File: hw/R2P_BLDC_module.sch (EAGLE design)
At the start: 59 parts, among them Q1 OPTIMOS, Q2 OPTIMOS, Q3 OPTIMOS, Q4 OPTIMOS, Q5 OPTIMOS, Q6 OPTIMOS, U1 STM32F103CX, U5 LD3985XX, X1 MICROMATCH-4

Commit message: H-bridge layout almost done
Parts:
- removed R3: 100k, rcl:R-EU_R0603
- removed U5: LD3985XX, st:LD3985XX
- added C14, C15, C16, C17: 100n, rcl:C-EUC0603
- added R11, R12: (no value), rcl:R-EU_R1206
- added R13, R14: 10, rcl:R-EU_R0603
- added U$10, U$12: INA193DBV, texas-instruments:INA193DBV
- added U$11: TPS73033, texas-instruments:TPS73033
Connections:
- net PWMAH renamed AH
- net PWMAL renamed AL
- removed net N$3: R3.2, U$1.TRI
- removed net PWMBH: U$8.PWMH
- removed net PWMBL: U$8.PWML
- removed net PWMCH: U$9.PWMH
- removed net PWMCL: U$9.PWML
- new net +A3V3: C14.1, C15.1, U$10SUPPLY.V+, U$12SUPPLY.V+, U1.VDD_A
- new net BH: U$8.PWMH, U1.PA9
- new net BL: U$8.PWML, U1.PB0
- new net CH: U$9.PWMH, U1.PA10
- new net CL: U$9.PWML, U1.PB1
- new net IA: C16.1, R13.1
- new net IB: C17.1, R14.1
- new net N$14: Q1G$1.D, Q1TH.TH, R11.1, U$12A.IN-
- new net N$16: Q2G$1.D, Q2TH.TH, R12.1, U$10A.IN-
- new net N$17: R13.2, U$12A.OUT
- new net N$19: R14.2, U$10A.OUT
- net +3V3: now also U$1.TRI, U$11.OUT; no longer R3.1, U1.VDD_A, U5.VOUT
- net +5V: now also U$11.EN, U$11.IN; no longer U5.INHIBIT, U5.VIN
- net +V: now also Q3TH.TH, R11.2, R12.2, U$10A.IN+, U$12A.IN+; no longer Q1G$1.D, Q2G$1.D
- net GND: now also C14.2, C15.2, C16.2, C17.2, U$10SUPPLY.V-, U$11.GND, U$12SUPPLY.V-, U$2.TH, U$8.TH, U$9.TH; no longer U5.GND
- net MA: now also Q4TH.TH
- net MB: now also Q5TH.TH
- net MC: now also Q6TH.TH
- net N$4: now also U$11.NR; no longer U5.BYPASS
- net UART_RX: now also U1.PB7; no longer U1.PA10
- net UART_TX: now also U1.PB6; no longer U1.PA9
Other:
- moved on the sheet: Q2, Q3, Q5, Q6, R10, R7, R8, R9

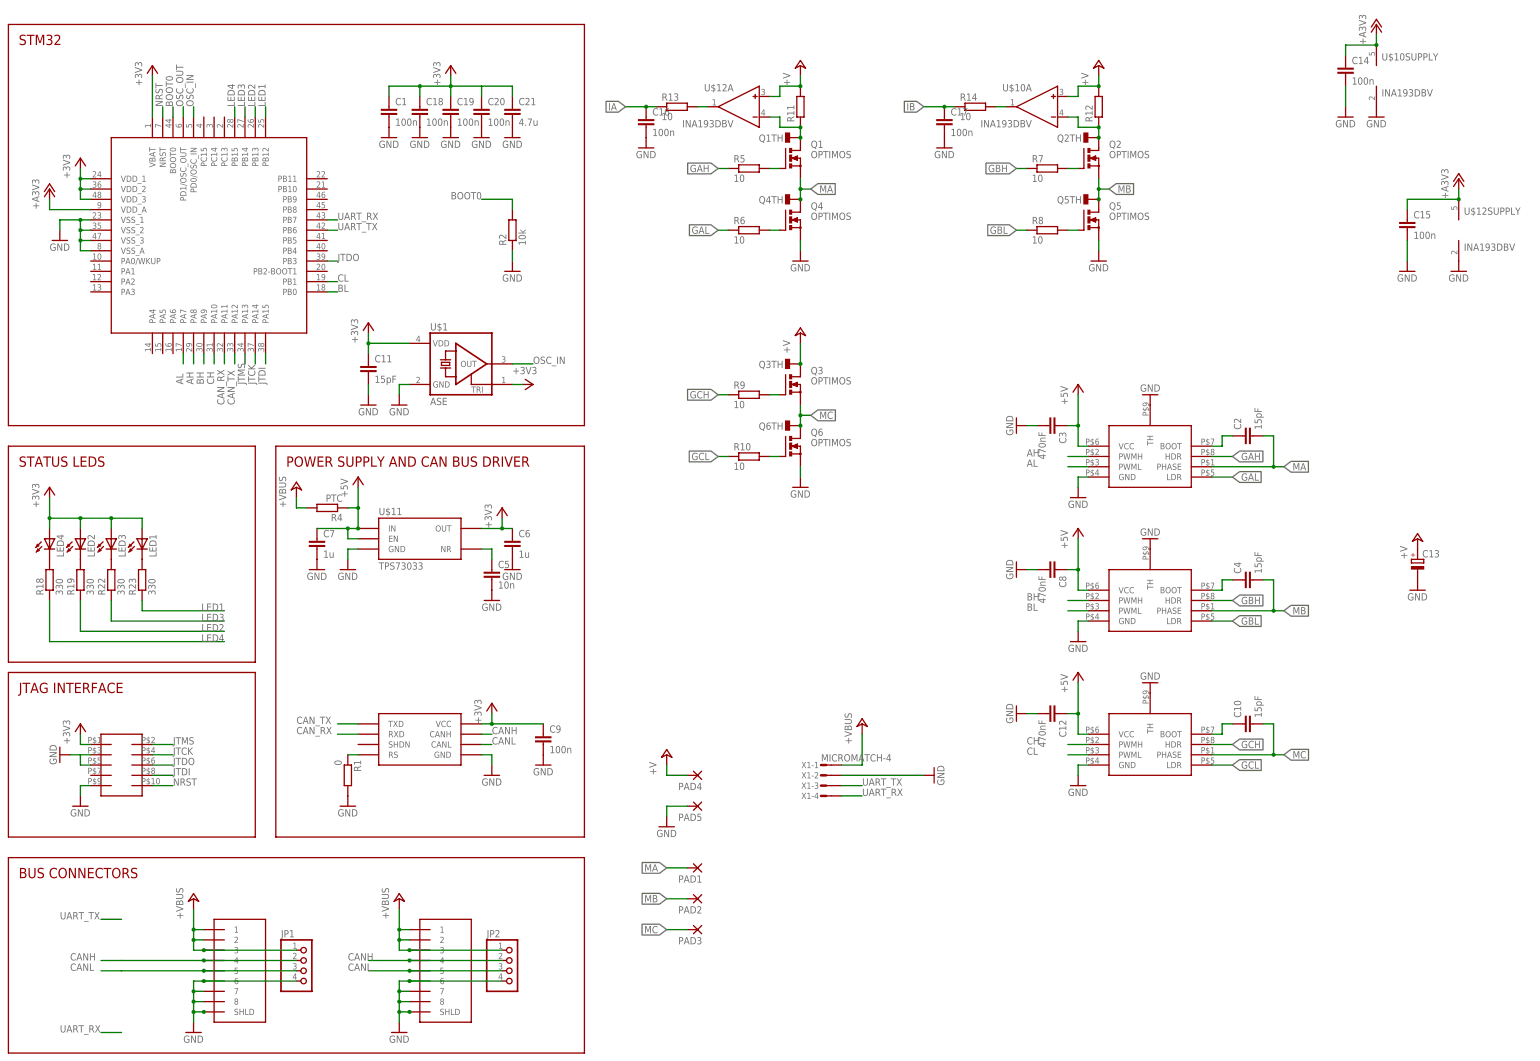
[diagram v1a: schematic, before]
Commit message: hall connector to be placed
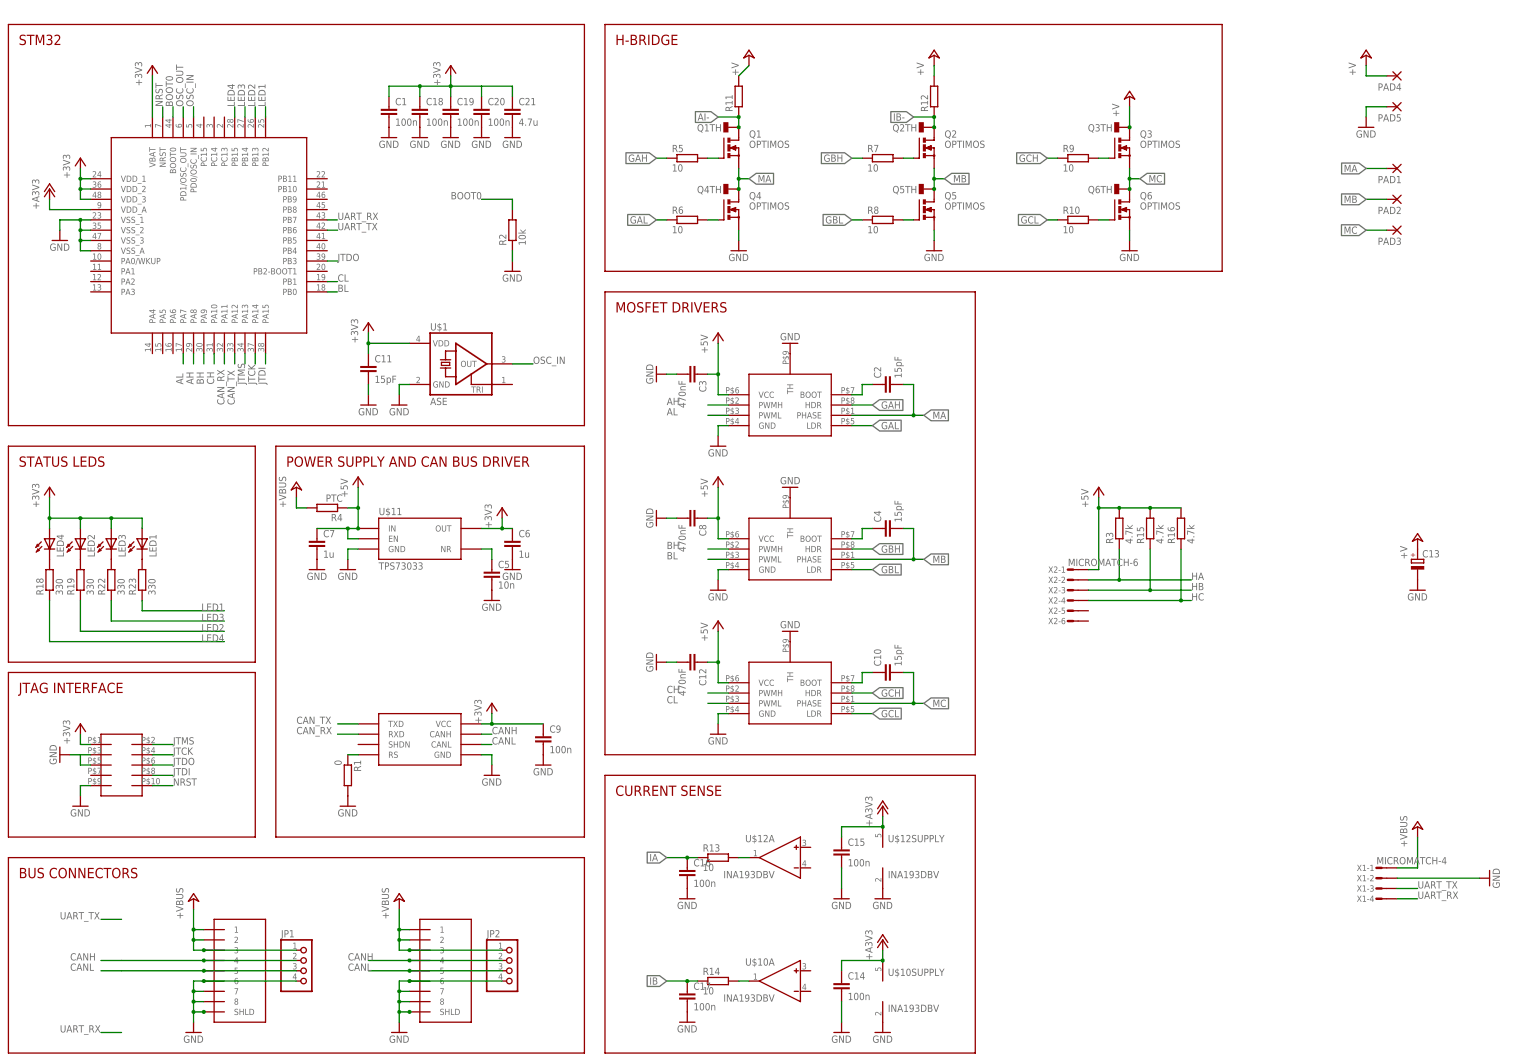
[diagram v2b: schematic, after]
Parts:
- added R15, R16, R3: 4.7k, rcl:R-EU_R0603
- added X2: MICROMATCH-6, apbteam_con-amp-micromatch:MICROMATCH-6
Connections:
- removed net N$14: Q1G$1.D, Q1TH.TH, R11.1, U$12A.IN-
- removed net N$16: Q2G$1.D, Q2TH.TH, R12.1, U$10A.IN-
- new net AI-: Q1G$1.D, Q1TH.TH, R11.1
- new net HA: R3.1, X2-2.S
- new net HB: R15.1, X2-3.S
- new net HC: R16.1, X2-4.S
- new net IB-: Q2G$1.D, Q2TH.TH, R12.1
- net +3V3: no longer U$1.TRI
- net +5V: now also R15.2, R16.2, R3.2, X2-1.S
- net +V: no longer U$10A.IN+, U$12A.IN+
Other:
- note added: "CURRENT SENSE"
- note added: "H-BRIDGE"
- note added: "MOSFET DRIVERS"
- moved on the sheet: C10, C12, C14, C15, C16, C17, C2, C3, C4, C8, PAD1, PAD2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
